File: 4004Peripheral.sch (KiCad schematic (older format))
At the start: 31 parts, among them J1 BUS, U1 Intel4289

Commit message: 修正
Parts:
- C1, C2: renamed from C?; value 10u -> 10u 16V; footprint (none) -> Capacitors_SMD:CP_Elec_4x4.5
- C4, C5, C6: renamed from C?; footprint (none) -> Capacitors_SMD:C_0603_HandSoldering
- J1: footprint (none) -> Pin_Headers:Pin_Header_Straight_2x20_Pitch2.54mm
- J2: renamed from J?; footprint (none) -> Pin_Headers:Pin_Header_Straight_1x02_Pitch2.54mm
- J3, J8: renamed from J?; footprint (none) -> Pin_Headers:Pin_Header_Straight_1x04_Pitch2.54mm
- J4: renamed from J?; footprint (none) -> Pin_Headers:Pin_Header_Straight_1x08_Pitch2.54mm
- J5, J6: renamed from J?; footprint (none) -> Pin_Headers:Pin_Header_Straight_1x01_Pitch2.54mm
- J7: renamed from J?; footprint Connectors:GS3 -> Connect:GS3
- R1, R2, R3, R4: renamed from R?; value 10k -> 2k; footprint (none) -> Resistors_SMD:R_0603_HandSoldering
- R10, R11, R12, R5, R6, R7, R8, R9: renamed from R?; footprint (none) -> Resistors_SMD:R_0603_HandSoldering
- SW0, SW1, SW2, SW3: renamed from SW?; footprint (none) -> Buttons_Switches_ThroughHole:SW_PUSH_6mm
- U1: footprint (none) -> Housings_DIP:DIP-40_W15.24mm_Socket
- U2: renamed from U?; footprint (none) -> Housings_DIP:DIP-24_W15.24mm_Socket
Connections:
- net A10: now also U2.19 (A10)
- net A8: now also U2.23 (A8)
- net A9: now also U2.22 (A9)
- net GND: now also J3.1 (Pin_1), J3.2 (Pin_2), J3.3 (Pin_3), J3.4 (Pin_4); no longer J2.1 (Pin_1), J2.2 (Pin_2)
- net VCC: now also J2.1 (Pin_1), J2.2 (Pin_2); no longer J3.1 (Pin_1), J3.2 (Pin_2), J3.3 (Pin_3), J3.4 (Pin_4)
- net A0: now reaches U1.23 (A0)
- net A0: now also U2.8 (A0)
- net A1: now reaches U1.24 (A1)
- net A1: now also U2.7 (A1)
- net A2: now reaches U1.25 (A2)
- net A2: now also U2.6 (A2)
- net A3: now reaches U1.26 (A3)
- net A3: now also U2.5 (A3)
- net A4: now reaches U1.27 (A4)
- net A4: now also U2.4 (A4)
- net A5: now reaches U1.28 (A5)
- net A5: now also U2.3 (A5)
- net A6: now reaches U1.29 (A6)
- net A6: now also U2.2 (A6)
- net A7: now reaches U1.30 (A7)
- net A7: now also U2.1 (A7)
- net at R8.2, U1.36 (IO3): no longer J8.4 (Pin_4)
- net at R7.2, U1.37 (IO2): no longer J8.3 (Pin_3)
- net at R6.2, U1.38 (IO1): no longer J8.2 (Pin_2)
- net at R5.2, U1.39 (IO0): no longer J8.1 (Pin_1)
- net at R1.2, R8.1, SW3.1: now also J8.4 (Pin_4)
- net at R2.2, R7.1, SW2.1: now also J8.3 (Pin_3)
- net at R3.2, R6.1, SW1.1: now also J8.2 (Pin_2)
- net at R4.2, R5.1, SW0.1: now also J8.1 (Pin_1)
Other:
- moved on the sheet: J8

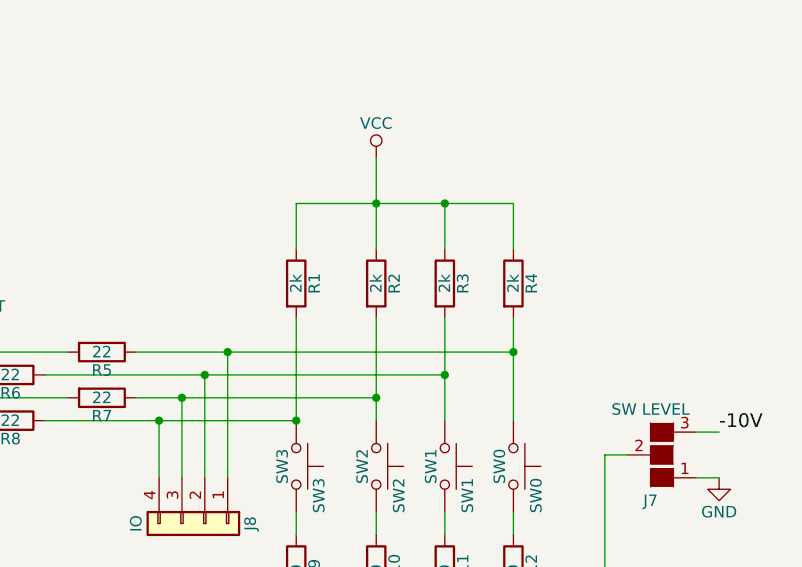
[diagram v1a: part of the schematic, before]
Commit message: 抵抗値変更
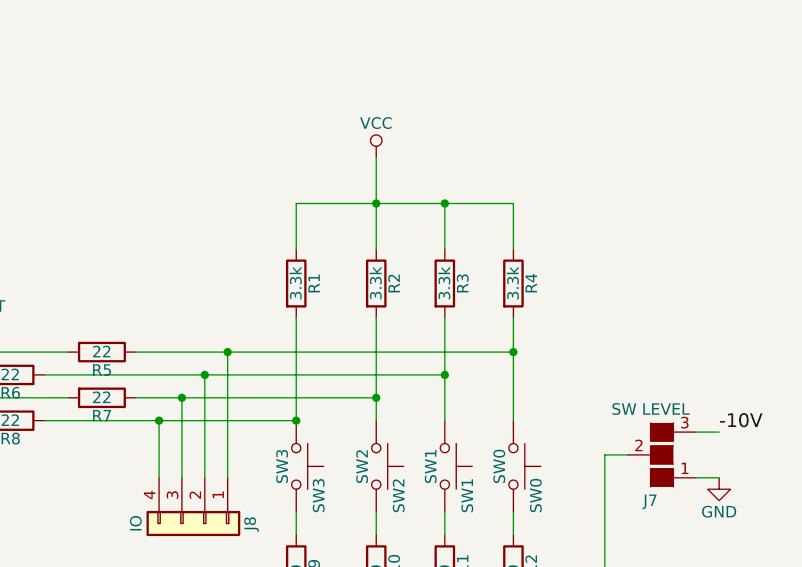
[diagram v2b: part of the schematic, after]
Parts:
- R1, R2, R3, R4: value 2k -> 3.3k
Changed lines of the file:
@@
 P 7750 5350
 F 0 "R1" V 7830 5350 50  0000 C CNN
-F 1 "2k" V 7750 5350 50  0000 C CNN
+F 1 "3.3k" V 7750 5350 50  0000 C CNN
 F 2 "Resistors_SMD:R_0603_HandSoldering" V 7680 5350 50  0001 C CNN
 F 3 "" H 7750 5350 50  0001 C CNN
@@
 P 8100 5350
 F 0 "R2" V 8180 5350 50  0000 C CNN
-F 1 "2k" V 8100 5350 50  0000 C CNN
+F 1 "3.3k" V 8100 5350 50  0000 C CNN
 F 2 "Resistors_SMD:R_0603_HandSoldering" V 8030 5350 50  0001 C CNN
 F 3 "" H 8100 5350 50  0001 C CNN
@@
 P 8400 5350
 F 0 "R3" V 8480 5350 50  0000 C CNN
-F 1 "2k" V 8400 5350 50  0000 C CNN
+F 1 "3.3k" V 8400 5350 50  0000 C CNN
 F 2 "Resistors_SMD:R_0603_HandSoldering" V 8330 5350 50  0001 C CNN
 F 3 "" H 8400 5350 50  0001 C CNN
@@
 P 8700 5350
 F 0 "R4" V 8780 5350 50  0000 C CNN
-F 1 "2k" V 8700 5350 50  0000 C CNN
+F 1 "3.3k" V 8700 5350 50  0000 C CNN
 F 2 "Resistors_SMD:R_0603_HandSoldering" V 8630 5350 50  0001 C CNN
 F 3 "" H 8700 5350 50  0001 C CNN

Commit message: ROMサイズ選択追加
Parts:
- added J9: ROM SIZE, Jumper:SolderJumper-3_P1.3mm_Open_RoundedPad1.0x1.5mm_NumberLabels, symbol 4004Peripheral-rescue:GS3
- C1, C2: symbol CP -> 4004Peripheral-rescue:CP
- C4, C5, C6: symbol C -> 4004Peripheral-rescue:C
- J1: symbol Conn_02x20_Odd_Even -> 4004Peripheral-rescue:Conn_02x20_Odd_Even
- J2: symbol Conn_01x02 -> 4004Peripheral-rescue:Conn_01x02
- J3, J8: symbol Conn_01x04 -> 4004Peripheral-rescue:Conn_01x04
- J4: symbol Conn_01x08 -> 4004Peripheral-rescue:Conn_01x08
- J5, J6: symbol Conn_01x01 -> 4004Peripheral-rescue:Conn_01x01
- J7: footprint Connect:GS3 -> Jumper:SolderJumper-3_P1.3mm_Open_RoundedPad1.0x1.5mm_NumberLabels; symbol GS3 -> 4004Peripheral-rescue:GS3
- R1, R10, R11, R12, R2, R3, R4, R5, R6, R7, R8, R9: symbol R -> 4004Peripheral-rescue:R
- SW0, SW1, SW2, SW3: symbol SW_Push -> 4004Peripheral-rescue:SW_Push
- U1: symbol Intel4289 -> 4004Peripheral-rescue:Intel4289
- U2: value 2716 -> 2716/2732; symbol 2716 -> 4004Peripheral-rescue:2716
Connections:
- net Vcc is gone; now on net VCC: U2.24 (Vcc)
- net VCC: now also J9.3 (G3); no longer U2.21 (Vpp)
- net A11: now reaches U1.34 (C3)
- net A11: now also J9.1 (G1)
- new net: J9.2 (G2), U2.21 (Vpp)
- no-connect marks 16 -> 15

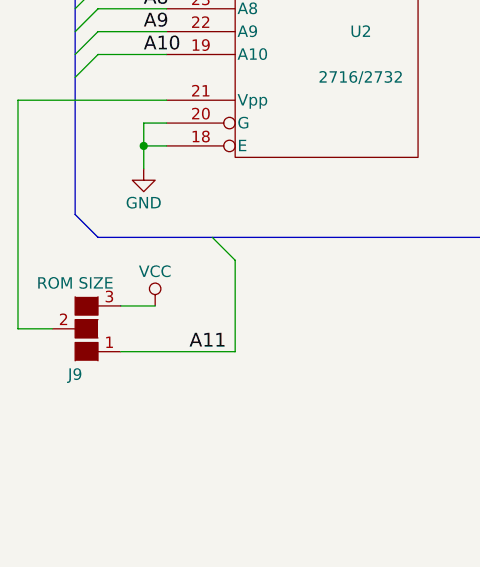
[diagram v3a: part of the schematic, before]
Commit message: minor silk change
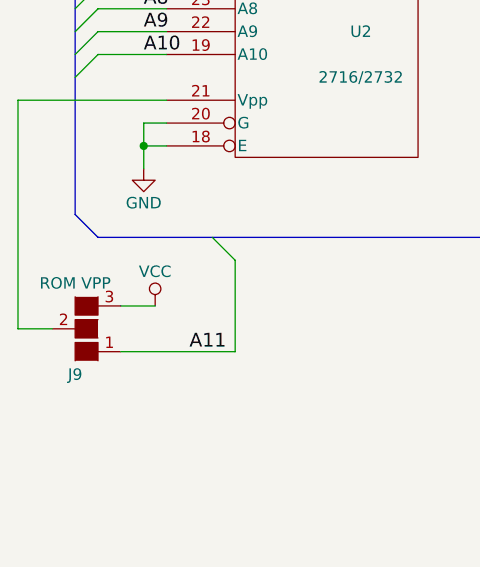
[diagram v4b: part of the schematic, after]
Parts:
- J9: value ROM SIZE -> ROM VPP
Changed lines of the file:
@@
 P 1650 5850
 F 0 "J9" H 1700 6050 50  0000 C CNN
-F 1 "ROM SIZE" H 1700 5651 50  0000 C CNN
+F 1 "ROM VPP" H 1700 5651 50  0000 C CNN
 F 2 "Jumper:SolderJumper-3_P1.3mm_Open_RoundedPad1.0x1.5mm_NumberLabels" V 1738 5776 50  0001 C CNN
 F 3 "" H 1650 5850 50  0001 C CNN
@@
 Wire Wire Line
 	2950 3000 2700 3000
+Connection ~ 2700 3000
 Wire Bus Line
 	1700 5450 4000 5450
@@
 Wire Bus Line
 	4100 4750 4100 5850
-Connection ~ 2700 3000
 $EndSCHEMATC
